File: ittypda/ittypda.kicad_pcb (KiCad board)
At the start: 2 copper layers, 105 x 66 mm, 149 parts, among them CN1 S2B-PH-SM4-TB, J1 USB_C_Receptacle_USB2.0_14P, J2 Conn_01x04_Pin, SW1 Switch, SW10 Switch, SW11 Switch, SW12 Switch, SW13 Switch, SW14 Switch, SW15 Switch, SW16 Switch, SW17 Switch, SW18 Switch, SW19 Switch, SW2 Switch, SW20 Switch, SW21 Switch, SW22 Switch, SW23 Switch, SW24 Switch, SW25 SLIDE SWITCH, SW26 Switch, SW27 Switch, SW28 Switch, SW29 Switch, SW3 Switch, SW30 Switch, SW31 Switch, SW32 Switch, SW33 Switch, SW34 Switch, SW36 Switch, SW37 Switch, SW38 Switch, SW39 Switch, SW4 Switch, SW41 Switch, SW42 Switch, SW43 Switch, SW44 Switch, SW45 Switch, SW46 Switch, SW47 Switch, SW48 Switch, SW49 Switch, SW5 Switch, SW50 Switch, SW51 Switch, SW52 Switch, SW53 Switch, SW54 Switch, SW55 Switch, SW56 Switch, SW57 Switch, SW58 Switch, SW59 Switch, SW6 Switch, SW60 Switch, SW61 Switch, SW7 Switch, SW8 Switch, SW9 Switch, U1 STM32F401RETx, U2 BQ24040DSQR, U3 TLV75801PDRV, Y1 16Mhz

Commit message: split power circuitry into seperate PCB part
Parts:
- added 3V3: Solder Pad 3.3V, TestPoint:TestPoint_Pad_D1.5mm, F.Cu at (90.3, 36.1)
- added 3V3: Solder Pad 3.3V, TestPoint:TestPoint_Pad_D1.5mm, F.Cu at (147.7, 36.1)
- added D+: Solder Pad D+, TestPoint:TestPoint_Pad_D1.5mm, F.Cu at (147.7, 42.5)
- added D+: Solder Pad D+, TestPoint:TestPoint_Pad_D1.5mm, F.Cu at (90.3, 42.5)
- added D-: Solder Pad D-, TestPoint:TestPoint_Pad_D1.5mm, F.Cu at (90.3, 45.7)
- added D-: Solder Pad D-, TestPoint:TestPoint_Pad_D1.5mm, F.Cu at (147.7, 45.7)
- added GND: Solder Pad GND, TestPoint:TestPoint_Pad_D1.5mm, F.Cu at (147.7, 39.3)
- added GND: Solder Pad GND, TestPoint:TestPoint_Pad_D1.5mm, F.Cu at (90.3, 39.3)
- added VBAT: Solder Pad VBAT, TestPoint:TestPoint_Pad_D1.5mm, F.Cu at (90.3, 32.9)
- added VBAT: Solder Pad VBAT, TestPoint:TestPoint_Pad_D1.5mm, F.Cu at (147.7, 32.9)
- CN1, J1, SW25: moved to F.Cu
- moved R2 104.8 mm to (166.8, 87.1)
- moved R3 104.8 mm to (166.8, 86.1)
- moved J1 104.2 mm to (162.6, 93.5), turned to 0 degrees
- moved LED1 104.0 mm to (153.0, 95.6), turned to 180 degrees
- moved R7 102.3 mm to (153.4, 94.3), turned to 180 degrees
- moved C11 93.8 mm to (163.6, 82.3)
- moved C12 93.8 mm to (163.4, 86.3)
- moved C13 93.8 mm to (156.4, 84.0)
- moved C14 93.8 mm to (156.3, 86.7)
- moved R6 93.8 mm to (162.1, 82.8)
- moved R8 93.8 mm to (157.9, 86.3)
- moved R9 93.8 mm to (158.9, 87.3)
- moved U2 93.8 mm to (162.5, 84.5)
- moved U3 93.8 mm to (158.3, 84.3)
- moved CN1 85.4 mm to (150.6, 70.3), turned to -90 degrees
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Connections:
- C14 pad 1: VBAT -> Net-(J6-Pin_1)
- J1 pad A6: USB_D+ -> Net-(J4-Pin_1)
- J1 pad A7: USB_D- -> Net-(J3-Pin_1)
- J1 pad B6: USB_D+ -> Net-(J4-Pin_1)
- J1 pad B7: USB_D- -> Net-(J3-Pin_1)
- R4 pad 2: USB_D- -> Net-(J9-Pin_1)
- R5 pad 2: USB_D+ -> Net-(J10-Pin_1)
- R8 pad 1: VBAT -> Net-(J6-Pin_1)
- SW25 pad 2: VBAT -> Net-(J6-Pin_1)
- SW25 pad 3: +3.3V -> Net-(J5-Pin_1)
- U1 pad 1: VBAT -> Net-(J7-Pin_1)
- U3 pad 1: VBAT -> Net-(J6-Pin_1)
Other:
- board size 105 x 66 mm -> 144.3 x 66 mm

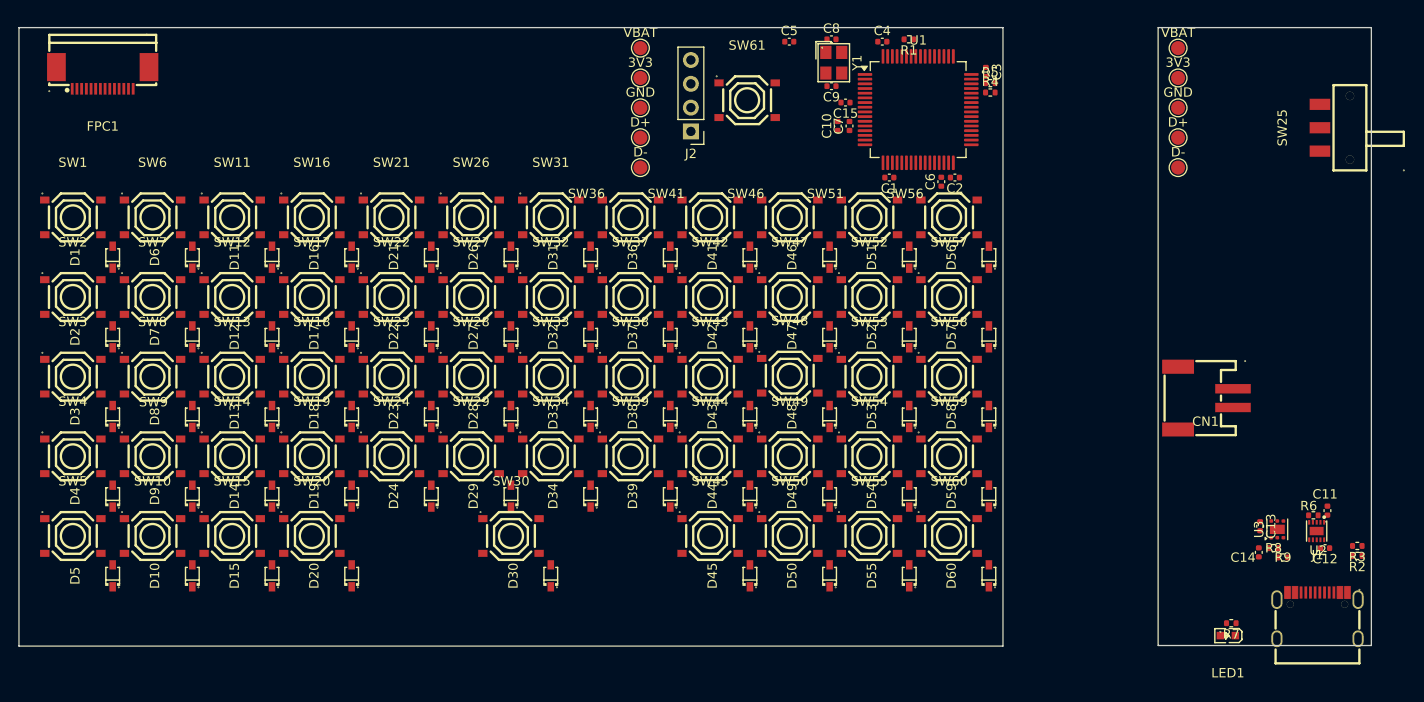
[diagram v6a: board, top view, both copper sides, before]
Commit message: add mouse bites
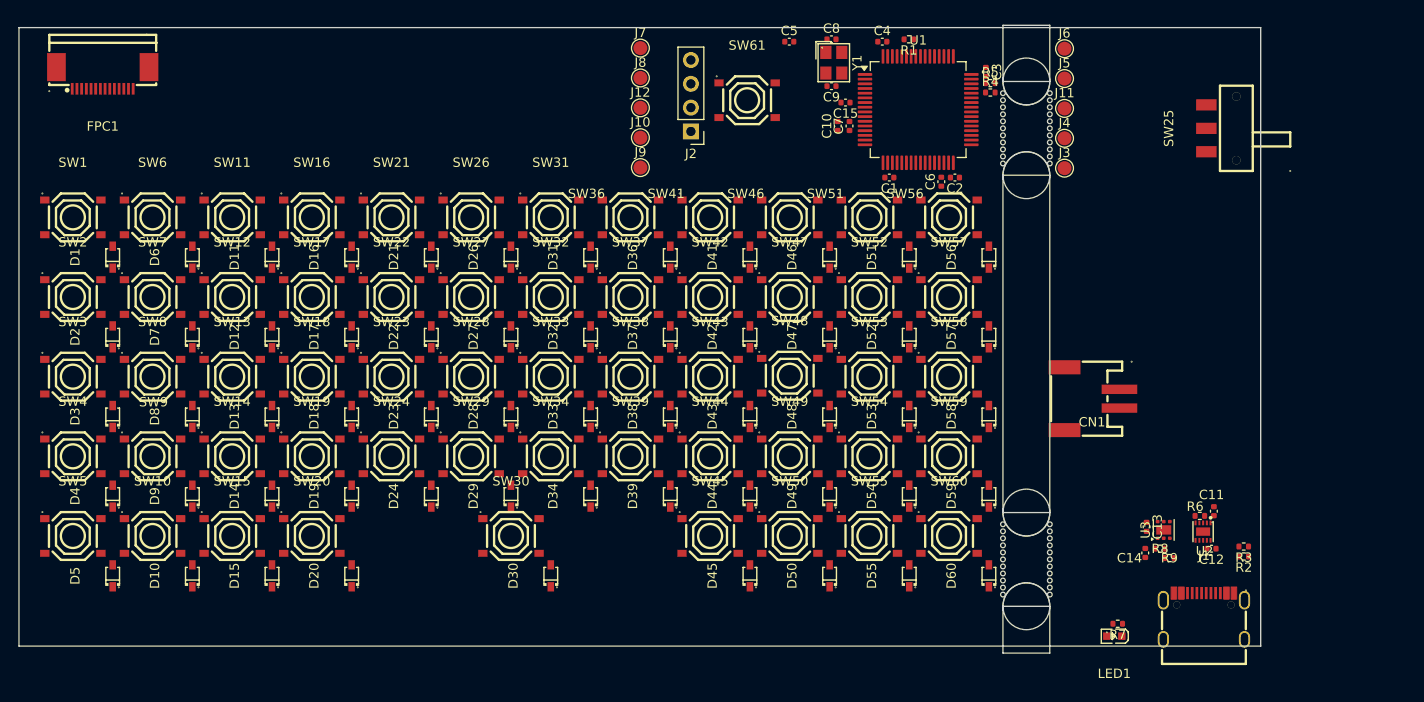
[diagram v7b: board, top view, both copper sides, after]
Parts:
- added mouse-bite-5mm-slot: VAL**, Panelization:mouse-bite-5mm-slot, F.Cu at (131.5, 41.5)
- added mouse-bite-5mm-slot: VAL**, Panelization:mouse-bite-5mm-slot, F.Cu at (131.5, 87.5)
- moved C11 12.1 mm to (151.5, 82.4)
- moved C12 12.1 mm to (151.3, 86.4)
- moved C13 12.1 mm to (144.3, 84.0)
- moved C14 12.1 mm to (144.2, 86.8)
- moved CN1 12.1 mm to (138.5, 70.3)
- moved J1 12.1 mm to (150.4, 93.6)
- moved J11 12.1 mm to (135.6, 39.4)
- moved J3 12.1 mm to (135.6, 45.8)
- moved J4 12.1 mm to (135.6, 42.6)
- moved J5 12.1 mm to (135.6, 36.2)
- moved J6 12.1 mm to (135.6, 33.0)
- moved LED1 12.1 mm to (140.9, 95.7)
- moved R2 12.1 mm to (154.7, 87.2)
- moved R3 12.1 mm to (154.7, 86.1)
- moved R6 12.1 mm to (150.0, 82.9)
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- renumbered D+ to J10, GND to J11, GND to J12, D- to J3, D+ to J4, 3V3 to J5, VBAT to J6, VBAT to J7, 3V3 to J8, D- to J9
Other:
- board size 144.3 x 66 mm -> 132.5 x 67 mm

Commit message: move mousebites to bottom of pcb
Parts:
- removed the mouse-bite-5mm-slot at (131.5, 41.5)
- removed the mouse-bite-5mm-slot at (131.5, 87.5)
- added mouse-bite-5mm-slot: VAL**, Panelization:mouse-bite-5mm-slot, F.Cu at (74.0, 98.0)
- added mouse-bite-5mm-slot: VAL**, Panelization:mouse-bite-5mm-slot, F.Cu at (116.5, 98.0)
- moved R2 91.6 mm to (70.7, 123.6), turned to 90 degrees
- moved R3 91.0 mm to (71.8, 123.6), turned to 90 degrees
- moved J1 89.9 mm to (64.3, 119.4), turned to -90 degrees
- moved C12 86.6 mm to (71.5, 120.2), turned to 90 degrees
- moved SW25 85.3 mm to (116.4, 119.6), turned to 0 degrees
- moved C11 85.0 mm to (75.5, 120.4), turned to 0 degrees
- moved U2 84.5 mm to (73.3, 119.3), turned to 90 degrees
- moved R6 83.2 mm to (75.0, 118.9), turned to -90 degrees
- moved R9 81.3 mm to (70.5, 115.7), turned to -90 degrees
- moved LED1 80.0 mm to (62.2, 109.8), turned to 90 degrees
- moved R8 79.5 mm to (71.5, 114.7), turned to -90 degrees
- moved R7 79.3 mm to (63.5, 110.2), turned to 90 degrees
- moved U3 78.9 mm to (73.5, 115.1), turned to 0 degrees
- moved C14 77.7 mm to (71.1, 113.1), turned to 180 degrees
- moved C13 76.3 mm to (73.9, 113.3), turned to 180 degrees
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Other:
- board size 132.5 x 67 mm -> 105 x 93.8 mm
